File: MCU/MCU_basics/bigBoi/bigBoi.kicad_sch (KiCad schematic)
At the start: 37 parts, among them J7 USB_B_Micro, SW1 Boot Switch, U1 STM32F469NIHx, Y1 8MHz

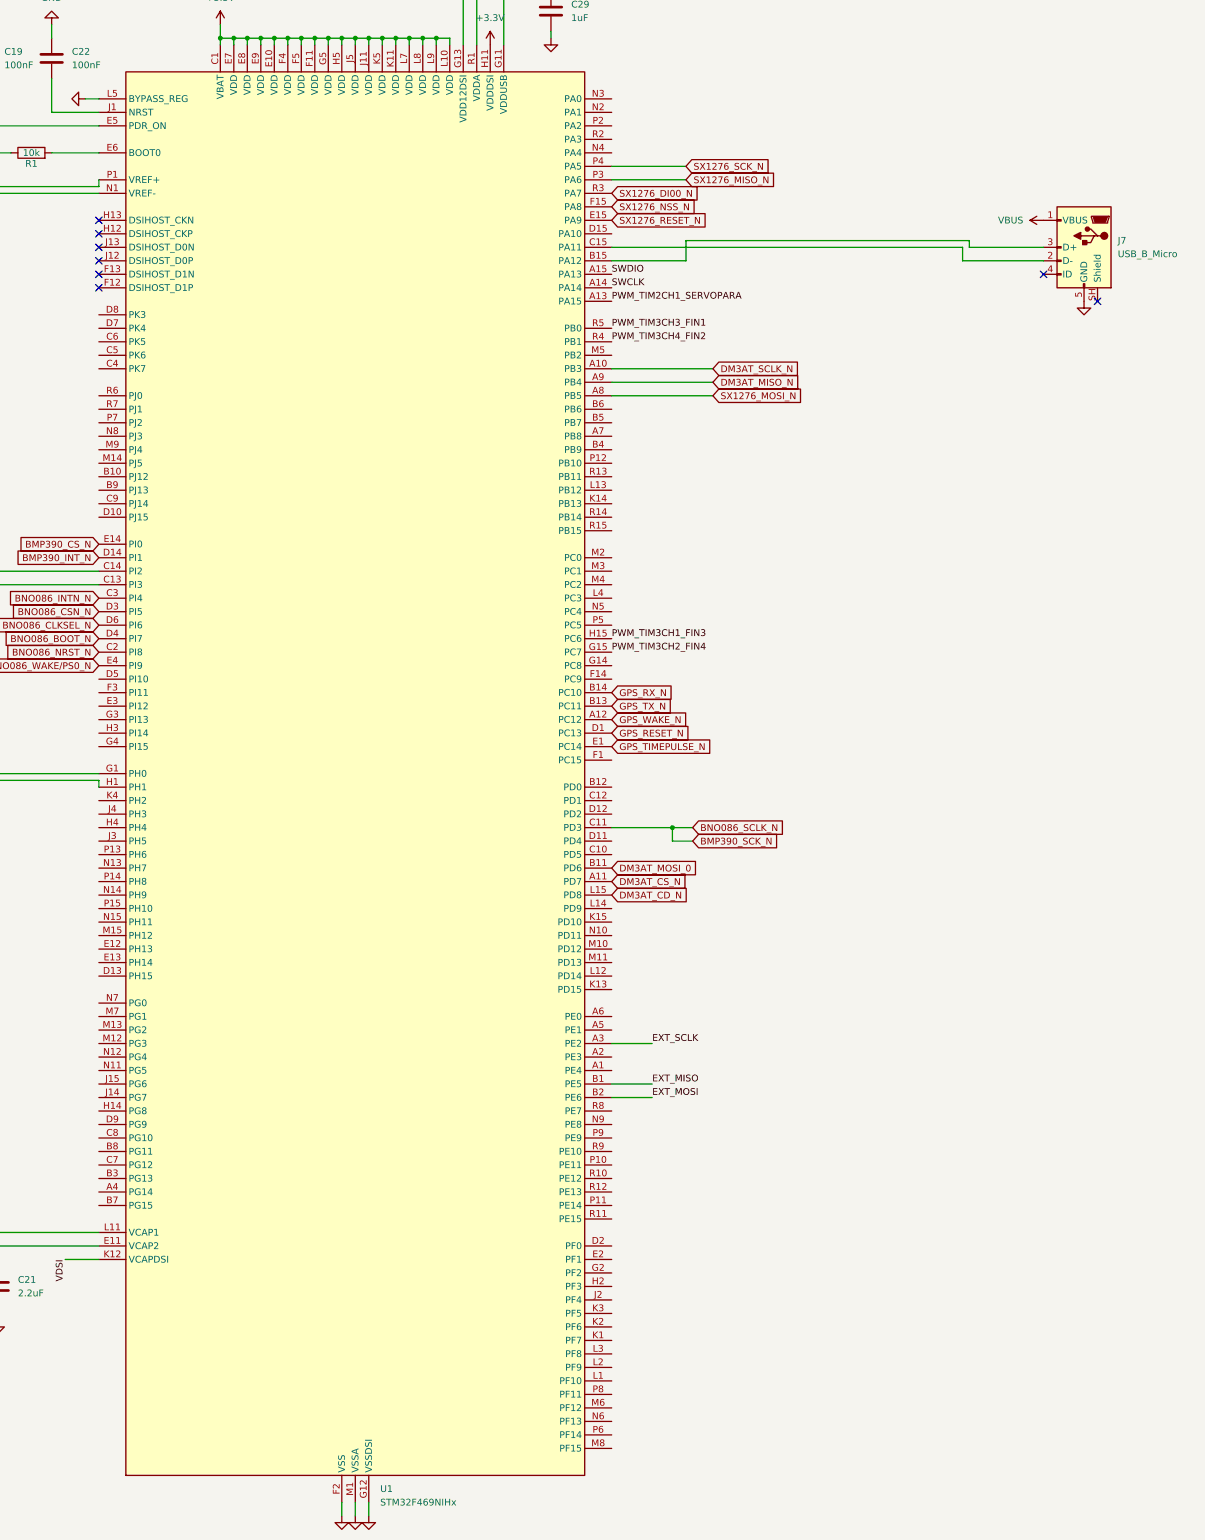
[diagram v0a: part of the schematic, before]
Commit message: most footprints assigned
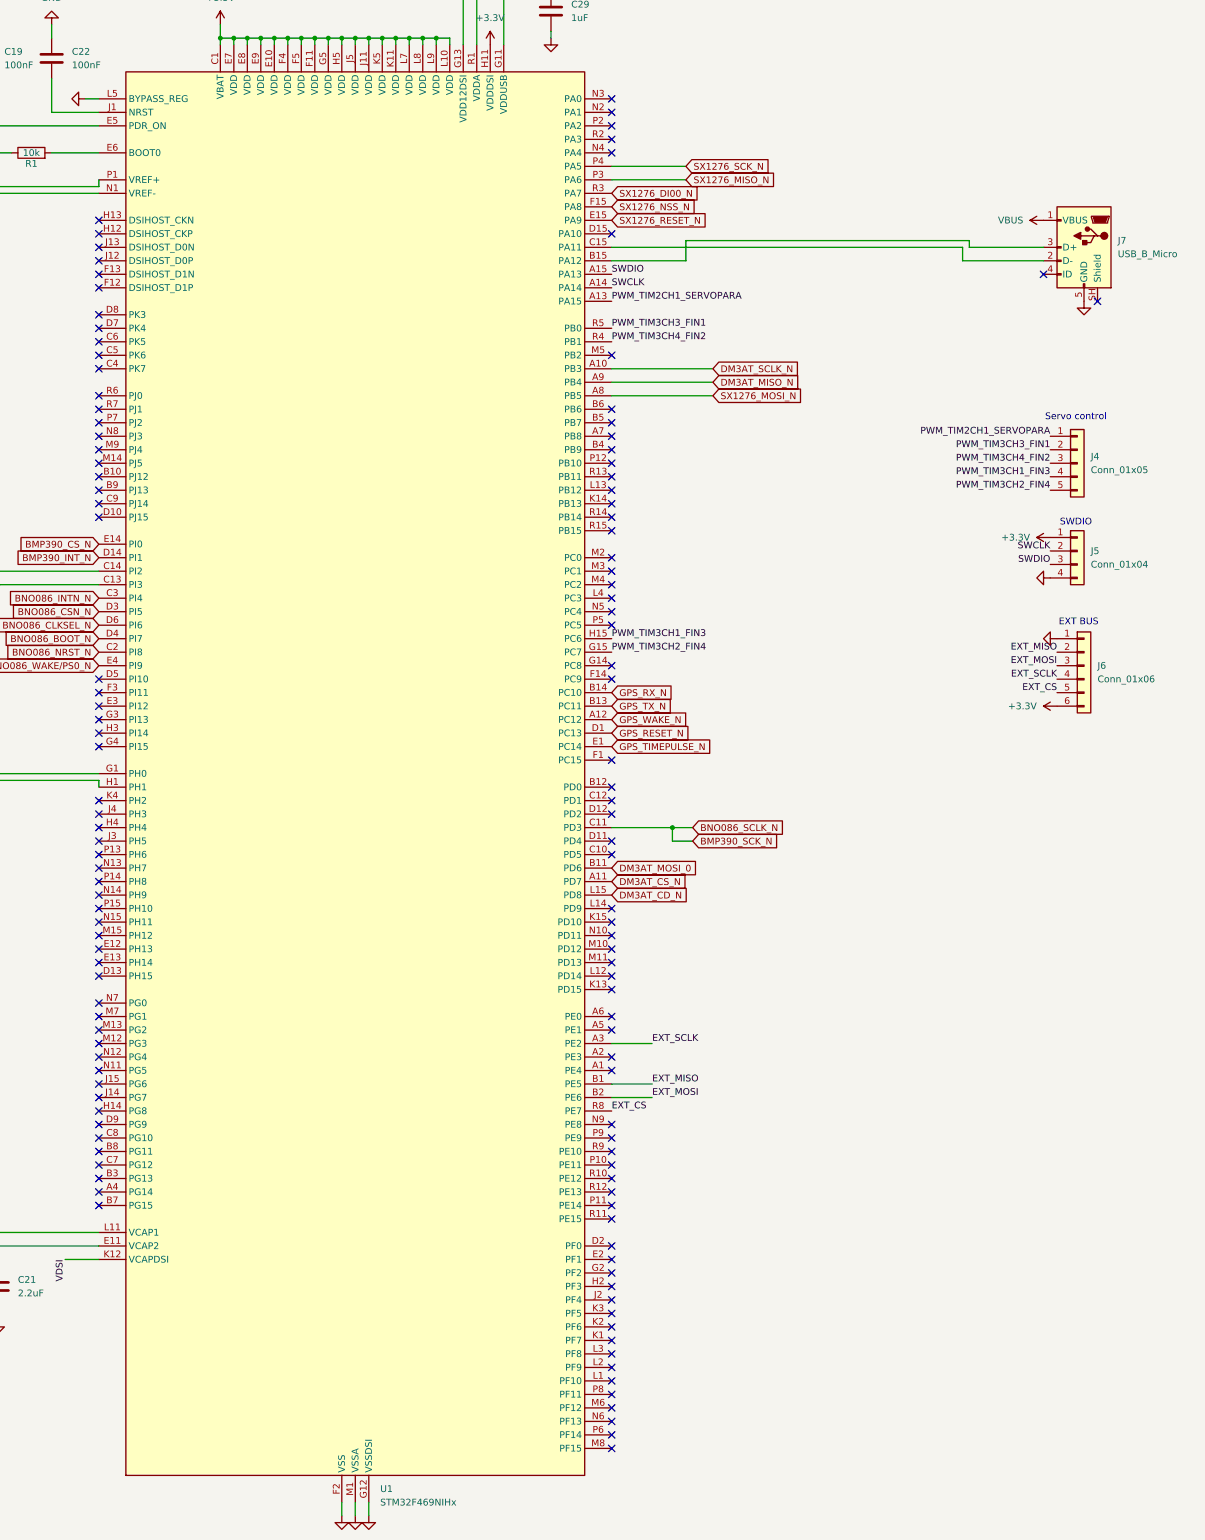
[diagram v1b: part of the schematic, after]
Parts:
- added J4: Conn_01x05, Connector_PinHeader_2.54mm:PinHeader_1x05_P2.54mm_Vertical, symbol Connector_Generic:Conn_01x05
- added J5: Conn_01x04, Connector_PinHeader_2.54mm:PinHeader_1x04_P2.54mm_Vertical, symbol Connector_Generic:Conn_01x04
- added J6: Conn_01x06, Connector_PinHeader_2.54mm:PinHeader_1x06_P2.54mm_Vertical, symbol Connector_Generic:Conn_01x06
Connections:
- net +3.3V: now also J5.1 (Pin_1), J6.6 (Pin_6)
- net EXT_MISO: now also J6.2 (Pin_2)
- net EXT_MOSI: now also J6.3 (Pin_3)
- net EXT_SCLK: now also J6.4 (Pin_4)
- net GND: now also J5.4 (Pin_4), J6.1 (Pin_1)
- net PWM_TIM2CH1_SERVOPARA: now also J4.1 (Pin_1)
- net PWM_TIM3CH1_FIN3: now also J4.4 (Pin_4)
- net PWM_TIM3CH2_FIN4: now also J4.5 (Pin_5)
- net PWM_TIM3CH3_FIN1: now also J4.2 (Pin_2)
- net PWM_TIM3CH4_FIN2: now also J4.3 (Pin_3)
- net SWCLK: now also J5.2 (Pin_2)
- net SWDIO: now also J5.3 (Pin_3)
- net EXT_CS: now reaches U1.R8 (PE7)
- net EXT_CS: now also J6.5 (Pin_5)
- no-connect marks 8 -> 125
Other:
- note added: "EXT BUS"
- note added: "SWDIO"
- note added: "Servo control"

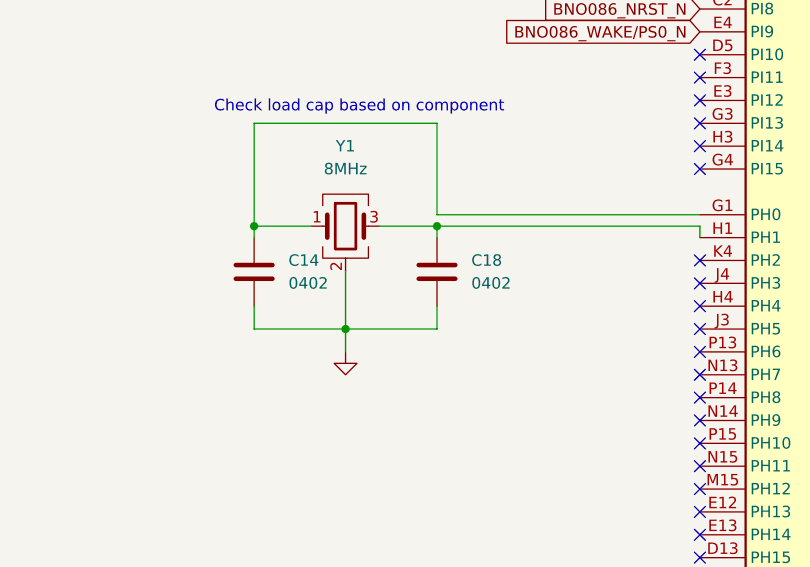
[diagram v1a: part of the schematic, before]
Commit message: Y2 fixed
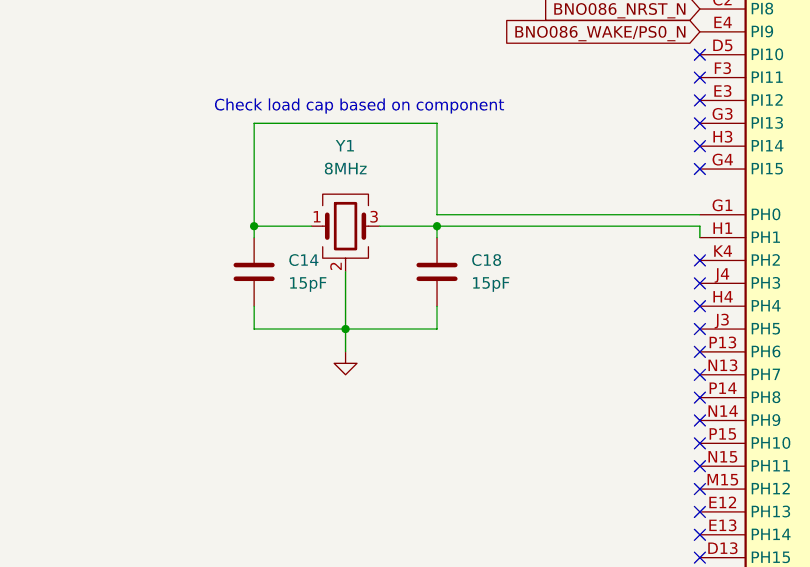
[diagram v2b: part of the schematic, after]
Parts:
- C14, C18: value 0402 -> 15pF
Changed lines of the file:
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@@
 			)
 		)
-		(property "Value" "0402"
+		(property "Value" "15pF"
 			(at 167.64 208.2799 0)
 			(show_name no)
@@
 			)
 		)
-		(property "Value" "0402"
+		(property "Value" "15pF"
 			(at 187.96 208.2799 0)
 			(show_name no)

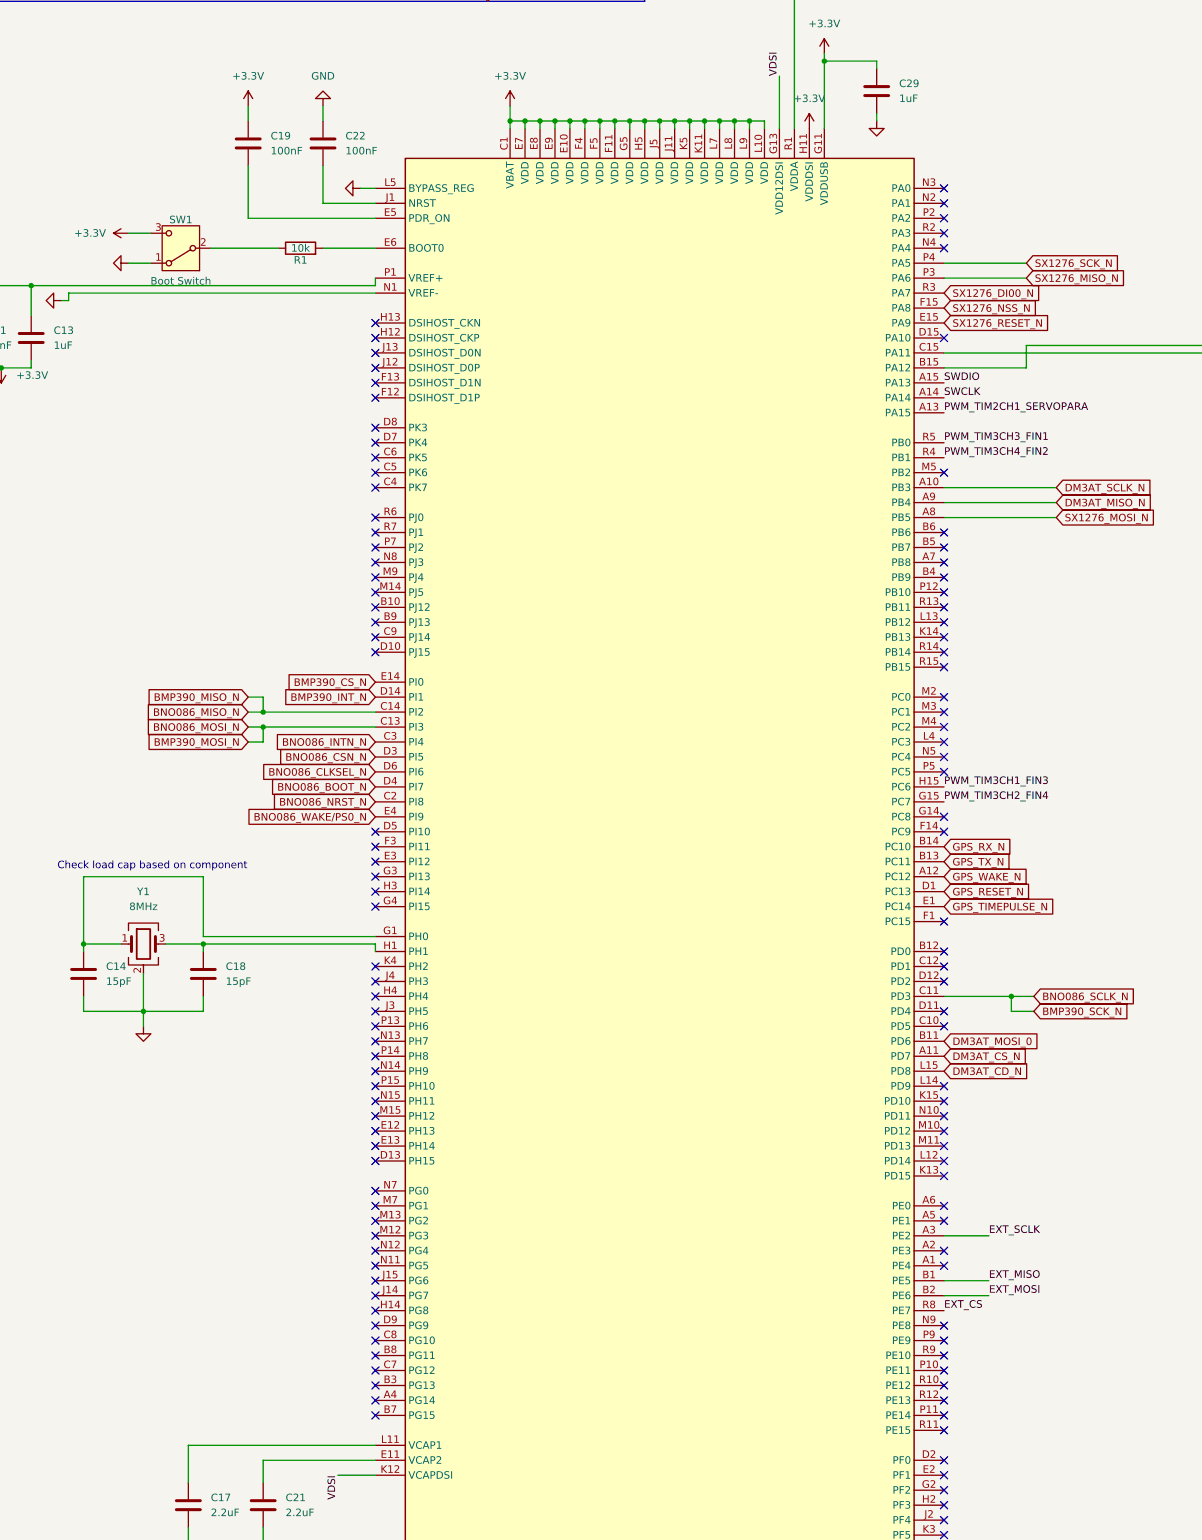
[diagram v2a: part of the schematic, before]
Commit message: decoupling cap placement
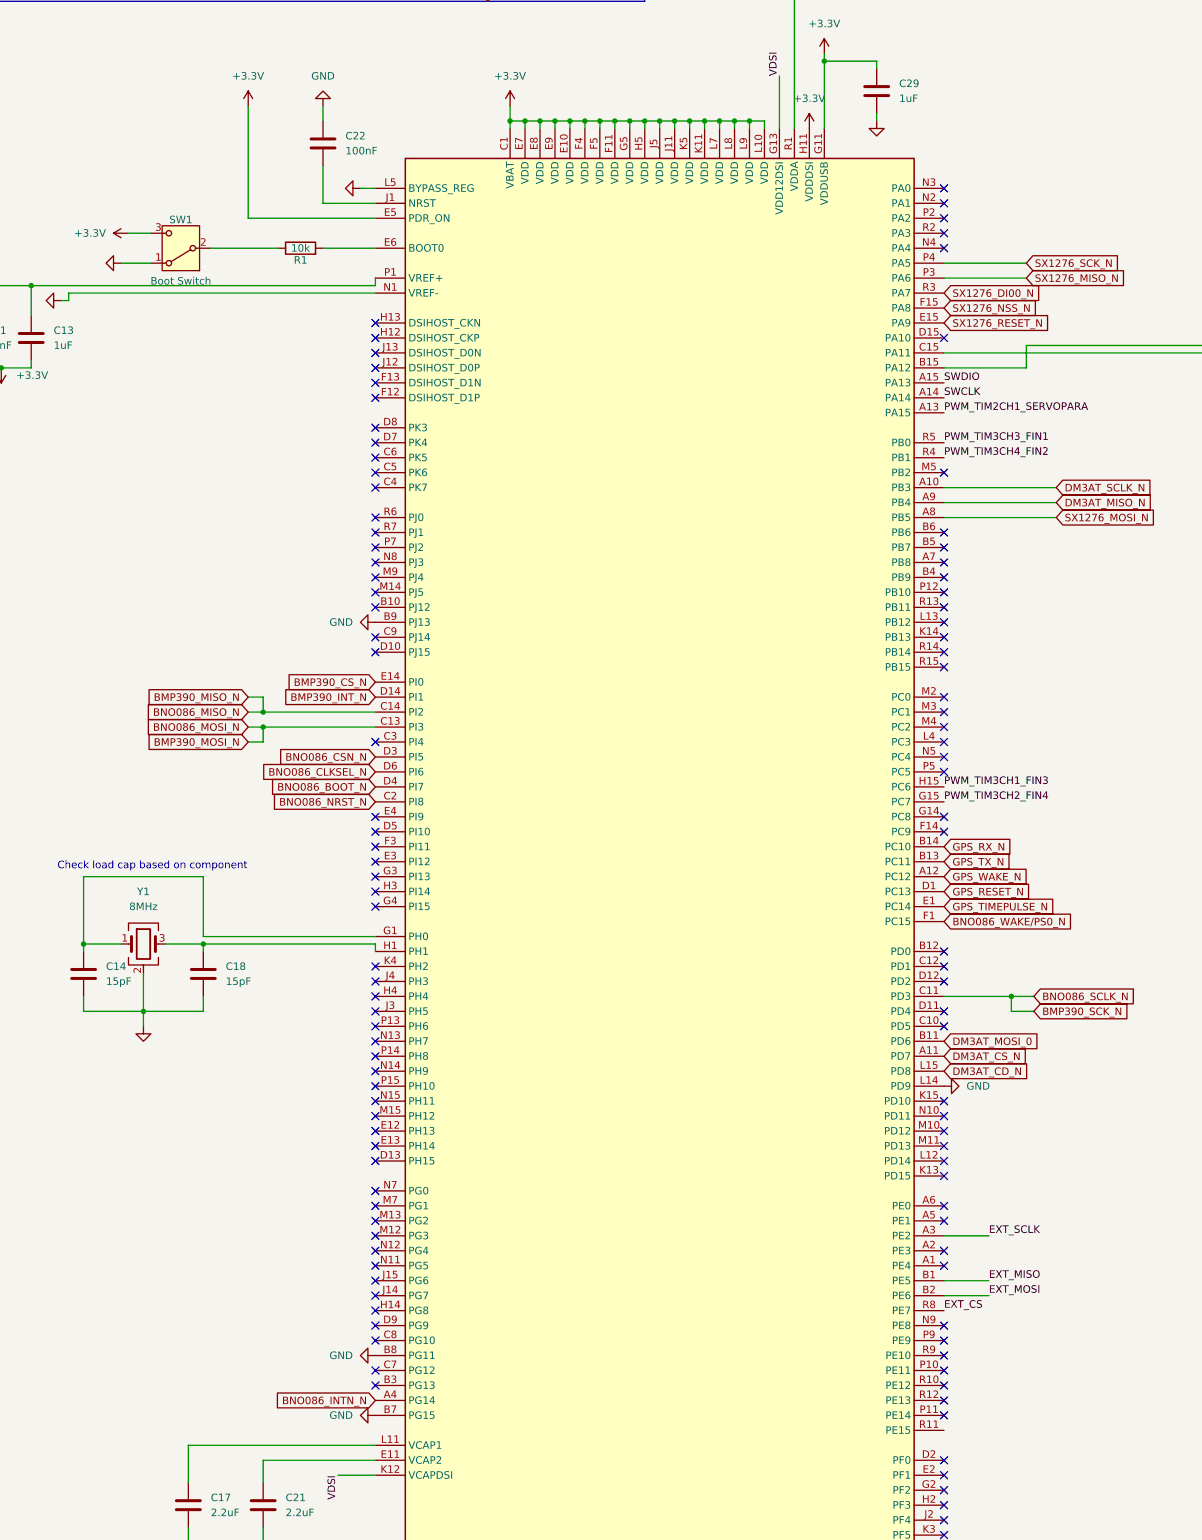
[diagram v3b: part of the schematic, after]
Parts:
- removed C19: 100nF, Capacitor_SMD:C_0402_1005Metric, symbol Device:C
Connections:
- net +3.3V: now also U1.E5 (PDR_ON)
- net BNO086_INTN_N: now also U1.A4 (PG14); no longer U1.C3 (PI4)
- net BNO086_WAKE/PS0_N: now also U1.F1 (PC15); no longer U1.E4 (PI9)
- net GND: now also U1.B7 (PG15), U1.B8 (PG11), U1.B9 (PJ13), U1.L14 (PD9)
- no-connect marks 125 -> 120
